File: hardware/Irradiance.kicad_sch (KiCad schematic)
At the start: 0 parts

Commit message: irradescence stuff
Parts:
- added C20: 0.1u, Capacitor_SMD:C_0603_1608Metric_Pad1.08x0.95mm_HandSolder, symbol Device:C
- added C21, C22: 100n, Capacitor_SMD:C_0603_1608Metric_Pad1.08x0.95mm_HandSolder, symbol Device:C
- added D5: TPD2EUSB30DRTR, LHRS_ICs:TPD2EUSB30DRTR, symbol lhrs_ics:TPD2EUSB30DRTR
- added J4: Nano-Fit 1x5, Connector_Molex:Molex_Nano-Fit_105313-xx05_1x05_P2.50mm_Horizontal, symbol Connector_Generic:Conn_01x05
- added R13, R14: 0, Resistor_SMD:R_0603_1608Metric_Pad0.98x0.95mm_HandSolder, symbol Device:R
- added R15: 100k, Resistor_SMD:R_0603_1608Metric_Pad0.98x0.95mm_HandSolder, symbol Device:R
- added R16, R18, R19: 1k, Resistor_SMD:R_0603_1608Metric_Pad0.98x0.95mm_HandSolder, symbol Device:R
- added R17: 10k, Resistor_SMD:R_0603_1608Metric_Pad0.98x0.95mm_HandSolder, symbol Device:R
- added TP2: TIA_OUT, TestPoint:TestPoint_Pad_D1.5mm, symbol Connector:TestPoint
- added TP3: PD_K, TestPoint:TestPoint_Pad_D1.5mm, symbol Connector:TestPoint
- added TP4: GNDA, TestPoint:TestPoint_Pad_D1.5mm, symbol Connector:TestPoint
- added U2: TLV9002QDRQ1, Package_SO:SOIC-8_3.9x4.9mm_P1.27mm, symbol lhrs_misc:TLV9002QDRQ1
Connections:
- net +3.3V: now also R15.1
- net GND: now also D5.3 (GND), R13.2
- net GNDA: now also C20.2, C22.2, J4.2 (Pin_2), J4.3 (Pin_3), R14.2, R18.2, TP4.1, U2.4 (V-), U2.5 (+)
- net IRRAD_ADC: now also C22.1, R19.2
- net IRRAD_DET: now also D5.2 (D-), J4.4 (Pin_4), R15.2
- net IRRAD_TEST: now also R17.1
- net VDDA: now also C20.1, U2.8 (V+)
- new net: R17.2, R18.1, U2.3 (+)
- new net OPB_FB: U2.6 (-), U2.7
- new net PD_K: C21.1, D5.1 (D+), J4.1 (Pin_1), R16.1, TP3.1, U2.2 (-)
- new net SHIELD: J4.5 (Pin_5), R13.1, R14.1
- new net TIA_OUT: C21.2, R16.2, R19.1, TP2.1, U2.1
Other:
- note added: "PD in photovoltaic mode: cathode to IN-, anode to GNDA. Vout = Isc x Rf (rises with sun). Rf 1k to start; final Rf = 2.5 V / Isc_fullsun measured behind the window. Cf 100n: ~1.6 kHz. Self-test: IRRAD_TEST high sets IN+ = 3.3 x 1k/11k = 0.30 V, so the output steps +0.30 V. GPIO Hi-Z normally."
- note added: "Test Points"
- note removed: "ADC Anti-Alias + Test Point"
- note removed: "IRRAD_TEST (MCU GPIO) -> R_test -> op-amp IN-. With PD dark/covered: Vout = (3.3 V / R_test) x Rf. e.g. R_test = 1M -> 3.3 uA known current. Proves the TIA + ADC chain works (validity bit). Leave GPIO Hi-Z in normal operation."
- note removed: "J?: harness to the irradiance breakout (2nd PCB). Pins: PD_A, PD_K (twisted pair), BRK_DET, GNDA, SHIELD. Use an LHRS Nano-Fit symbol (ask harness lead for count). SHIELD: 0R to GND (fit) + 0R to GNDA (DNP), same scheme as the strain gauge J8. Terminate the shield at THIS end only. BRK_DET: breakout ties it to GNDA. 10k pull-up to +3.3V here -> IRRAD_DET. High = breakout missing (fault flag)."
- note removed: "Notes"
- note removed: "Photodiode in photovoltaic mode (0 V bias): PD_A -> op-amp IN-, PD_K -> GNDA, IN+ -> GNDA. Rf from OUT to IN-, Cf across Rf. Vout = Isc x Rf. Pick Rf so full sun (~1000 W/m2) gives ~2.5 V: Rf = 2.5 V / Isc_fullsun. MEASURE Isc_fullsun first (meter in uA/mA mode, PD shorted, in real sun, behind the window). Cf: fc = 1/(2 pi Rf Cf) ~ 100 Hz (CAN rate 10 Hz). Op-amp: rail-to-rail out, low offset, ca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"
- note removed: "Rs ~1k + 100 nF to GNDA into IRRAD_ADC (PA3 = ADC1_IN4, verify in CubeMX). Test points: TIA_OUT, PD_A, GNDA."
- note removed: "Self-Test Injection"
- note removed: "TPD2EUSB30DRTR (ELC parts list, C97502) on PD_A + PD_K, pin 3 -> GND. Place right at the connector. Optional 2nd: BRK_DET."
- note removed: "Why analog instead of I2C (old TSL2591 breakout): - Old board ran I2C over a 6" off-board harness; motor noise at comp + bus capacitance made it unreliable (Notion Blackbody v1.0.0, #array 10/5). - TSL2591 has a fixed address (0x29), so multiple sensors needed a mux/translator. - A silicon photodiode responds ~430-1100 nm, peak ~900 nm: same band the solar cells use (Aarav: 300-1100 nm, peak 800-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"
- company: Longhorn Racing Solar - VCAT Telemetry -> (none)
- title: Irradiance Front End -> (none)

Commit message: check breakout board layout
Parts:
- removed C20: 0.1u, Capacitor_SMD:C_0603_1608Metric_Pad1.08x0.95mm_HandSolder, symbol Device:C
- removed C21, C22: 100n, Capacitor_SMD:C_0603_1608Metric_Pad1.08x0.95mm_HandSolder, symbol Device:C
- removed D5: TPD2EUSB30DRTR, LHRS_ICs:TPD2EUSB30DRTR, symbol lhrs_ics:TPD2EUSB30DRTR
- removed R13, R14: 0, Resistor_SMD:R_0603_1608Metric_Pad0.98x0.95mm_HandSolder, symbol Device:R
- removed R15: 100k, Resistor_SMD:R_0603_1608Metric_Pad0.98x0.95mm_HandSolder, symbol Device:R
- removed R16, R18, R19: 1k, Resistor_SMD:R_0603_1608Metric_Pad0.98x0.95mm_HandSolder, symbol Device:R
- removed R17: 10k, Resistor_SMD:R_0603_1608Metric_Pad0.98x0.95mm_HandSolder, symbol Device:R
- removed U2: TLV9002QDRQ1, Package_SO:SOIC-8_3.9x4.9mm_P1.27mm, symbol lhrs_misc:TLV9002QDRQ1
- added D5: D5V0P4UR6SO-7, LHRS_ICs:D5V0P4UR6SO-7, symbol lhrs_ics:D5V0P4UR6SO-7
- TP2: value TIA_OUT -> SDA
- TP3: value PD_K -> SCL
- TP4: value GNDA -> INT
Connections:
- net SHIELD is gone; now on net GND: J4.5 (Pin_5)
- net +3.3V: now also J4.1 (Pin_1), D5.5
- net GND: now also D5.2
- removed net GNDA: J4.2 (Pin_2), J4.3 (Pin_3), TP4.1
- net IRRAD_DET renamed IRRAD_INT
- net IRRAD_INT: now also TP4.1, D5.6
- net PD_K renamed I2C_SCL
- net I2C_SCL: now also J4.3 (Pin_3), D5.3; no longer J4.1 (Pin_1)
- net TIA_OUT renamed I2C_SDA
- net I2C_SDA: now also J4.2 (Pin_2), D5.1
- no-connect marks 0 -> 1
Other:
- note added: "+3.3V"
- note added: "GND"
- note added: "SCL"
- note added: "SDA"
- note added: "~{INT}"
- note removed: "PD in photovoltaic mode: cathode to IN-, anode to GNDA. Vout = Isc x Rf (rises with sun). Rf 1k to start; final Rf = 2.5 V / Isc_fullsun measured behind the window. Cf 100n: ~1.6 kHz. Self-test: IRRAD_TEST high sets IN+ = 3.3 x 1k/11k = 0.30 V, so the output steps +0.30 V. GPIO Hi-Z normally."
- note removed: "Transimpedance Amplifier"

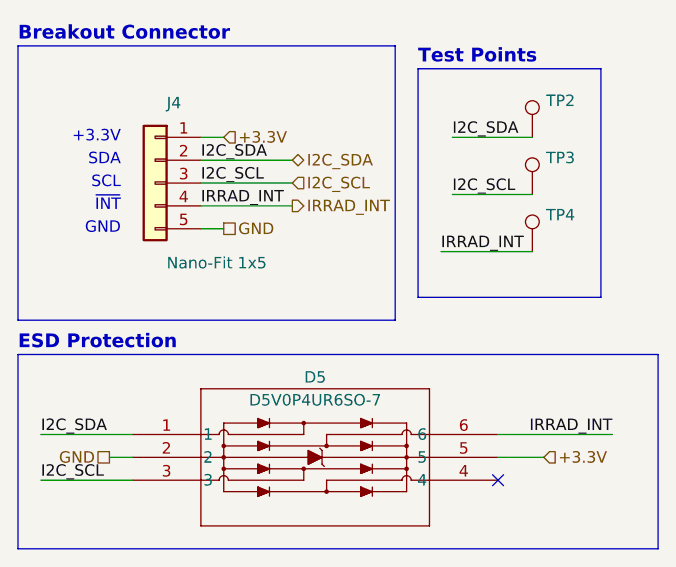
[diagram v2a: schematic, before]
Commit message: Main board placement + silkscreen, breakout ground plane, DRC rule updates
- Grouped placement and condensed outline (2 mm rounded corners)
- Silkscreen refs moved next to their parts, pin labels added
- Interrupt removed from main board and breakout (test point instead)
- Breakout: B.Cu ground plane + stitching vias
- Default clearance / hole clearance lowered to 0.15 mm
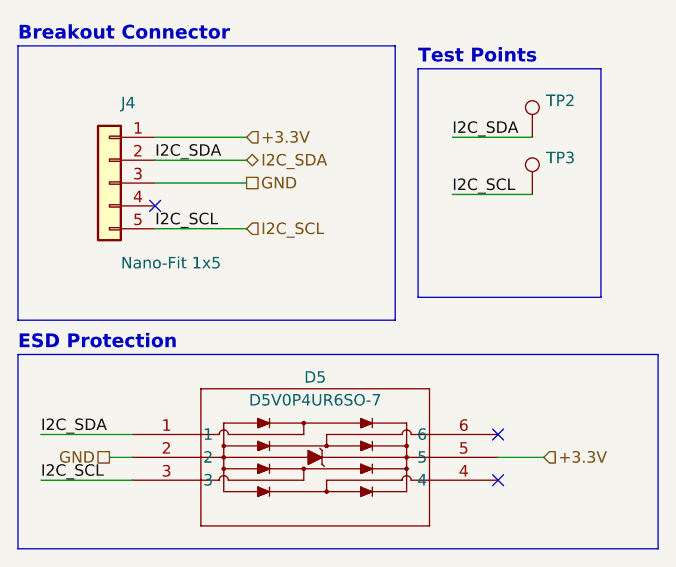
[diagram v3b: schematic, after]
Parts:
- removed TP4: INT, TestPoint:TestPoint_Pad_D1.5mm, symbol Connector:TestPoint
- J4: P/N (none) -> 1053131105
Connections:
- net GND: now also J4.3 (Pin_3); no longer J4.5 (Pin_5)
- net I2C_SCL: now also J4.5 (Pin_5); no longer J4.3 (Pin_3)
- net IRRAD_INT: no longer names the net of J4.4 (Pin_4)
- net IRRAD_INT: no longer D5.6
- no-connect marks 1 -> 3
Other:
- note removed: "+3.3V"
- note removed: "GND"
- note removed: "SCL"
- note removed: "SDA"
- note removed: "~{INT}"
- moved on the sheet: J4
